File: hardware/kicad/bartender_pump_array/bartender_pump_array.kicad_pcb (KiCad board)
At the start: 2 copper layers, 56 x 61.8 mm, 43 parts, among them J1 Pump 1, J10 Pump 10, J11 12V INPUT, J12 Conn_01x12_Female, J2 Pump 2, J3 Pump 3, J4 Pump 4, J5 Pump 5, J6 Pump 6, J7 Pump 7, J8 Pump 8, J9 Pump 9, Q1 TIP120, Q10 TIP120, Q2 TIP120, Q3 TIP120, Q4 TIP120, Q5 TIP120, Q6 TIP120, Q7 TIP120, Q8 TIP120, Q9 TIP120

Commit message: Got wifi up and running, started work on the Mini
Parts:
- removed REF**: OSHW-Symbol_6.7x6mm_SilkScreen, Symbol:OSHW-Symbol_6.7x6mm_SilkScreen
- added H1: MountingHole_Pad, MountingHole:MountingHole_3.2mm_M3_Pad, F.Cu at (31.0, 45.5)
- added H2: MountingHole_Pad, MountingHole:MountingHole_3.2mm_M3_Pad, F.Cu at (62.9, 89.0)
- added R11: R_Small_US, Resistor_SMD:R_0603_1608Metric, B.Cu at (50.7, 85.2)
- added R12: R_Small_US, Resistor_SMD:R_0603_1608Metric, B.Cu at (50.7, 76.5)
- added R13: R_Small_US, Resistor_SMD:R_0603_1608Metric, B.Cu at (50.7, 67.8)
- added R14: R_Small_US, Resistor_SMD:R_0603_1608Metric, B.Cu at (50.7, 59.1)
- added R15: R_Small_US, Resistor_SMD:R_0603_1608Metric, B.Cu at (50.6, 50.5)
- added R16: R_Small_US, Resistor_SMD:R_0603_1608Metric, B.Cu at (59.2, 85.1)
- added R17: R_Small_US, Resistor_SMD:R_0603_1608Metric, B.Cu at (59.2, 76.5)
- added R18: R_Small_US, Resistor_SMD:R_0603_1608Metric, B.Cu at (59.2, 67.8)
- added R19: R_Small_US, Resistor_SMD:R_0603_1608Metric, B.Cu at (59.1, 59.8)
- added R20: R_Small_US, Resistor_SMD:R_0603_1608Metric, B.Cu at (59.1, 50.5)
- added U1: MCP23017_SO, Package_SO:SOIC-28W_7.5x17.9mm_P1.27mm, F.Cu at (34.9, 62.4)
- D1, D10, D2, D3, D4, D5, D6, D7, D8, D9: value DIODE -> 1N4148W; footprint Diode_THT:D_DO-41_SOD81_P5.08mm_Vertical_AnodeUp -> Diode_SMD:D_SOD-123; moved to B.Cu
- J1: value Pump 1 -> 1
- J10: value Pump 10 -> 10
- J11: value 12V INPUT -> 12V
- J12: value Conn_01x12_Female -> Conn_01x04_Female; footprint Connector_JST:JST_XH_B12B-XH-A_1x12_P2.50mm_Vertical -> Connector_JST:JST_XH_B4B-XH-A_1x04_P2.50mm_Vertical
- J2: value Pump 2 -> 2
- J3: value Pump 3 -> 3
- J4: value Pump 4 -> 4
- J5: value Pump 5 -> 5
- J6: value Pump 6 -> 6
- J7: value Pump 7 -> 7
- J8: value Pump 8 -> 8
- J9: value Pump 9 -> 9
- Q1, Q10, Q2, Q3, Q4, Q5, Q6, Q7, Q8, Q9: value TIP120 -> AO3400A; footprint Package_TO_SOT_THT:TO-220-3_Vertical -> Package_TO_SOT_SMD:SOT-23; moved to B.Cu
- R1, R10, R2, R3, R4, R5, R6, R7, R8, R9: footprint Resistor_THT:R_Axial_DIN0207_L6.3mm_D2.5mm_P5.08mm_Vertical -> Resistor_SMD:R_0603_1608Metric; moved to B.Cu
- moved R6 30.6 mm to (55.9, 85.1)
- moved R7 26.5 mm to (55.9, 76.5)
- moved J6 23.6 mm to (57.0, 83.2)
- moved R8 22.8 mm to (55.9, 67.8)
- moved J7 22.5 mm to (57.0, 74.5)
- moved J8 21.5 mm to (57.0, 65.9)
- moved J9 20.7 mm to (57.0, 57.2)
- moved J10 20.2 mm to (57.0, 48.6)
- moved R9 20.2 mm to (55.9, 59.8)
- moved D6 20.1 mm to (54.6, 81.9)
- moved J11 19.8 mm to (40.1, 80.4), turned to -90 degrees
- moved D7 18.9 mm to (54.7, 73.3)
- moved R10 18.2 mm to (55.9, 50.5)
- moved D8 18.1 mm to (54.7, 64.6)
- moved Q6 17.9 mm to (60.5, 82.0), turned to 0 degrees
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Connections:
- J12 pad 1: /P1 -> Net-(J12-Pad1)
- J12 pad 2: /P2 -> Net-(J12-Pad2)
- J12 pad 3: /P3 -> Net-(J12-Pad3)
- J12 pad 4: /P4 -> GND
- R1 pad 1: /P1 -> Net-(R1-Pad1)
- R10 pad 1: /P10 -> Net-(R10-Pad1)
- R2 pad 1: /P2 -> Net-(R2-Pad1)
- R3 pad 1: /P3 -> Net-(R3-Pad1)
- R4 pad 1: /P4 -> Net-(R4-Pad1)
- R5 pad 1: /P5 -> Net-(R5-Pad1)
- R6 pad 1: /P6 -> Net-(R6-Pad1)
- R7 pad 1: /P7 -> Net-(R7-Pad1)
- R8 pad 1: /P8 -> Net-(R8-Pad1)
- R9 pad 1: /P9 -> Net-(R9-Pad1)
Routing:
- net /12v: track 306.7 -> 144.7 mm, vias 1 -> 0
- net Net-(R6-Pad2): track 88.0 -> 4.23 mm
- net GND: track 219.7 -> 145.1 mm
- net Net-(R7-Pad2): track 74.9 -> 4.29 mm
- net Net-(R6-Pad1): track 0.00 -> 70.4 mm, vias 0 -> 1
- net Net-(R7-Pad1): track 0.00 -> 62.7 mm, vias 0 -> 1
- net Net-(R8-Pad2): track 61.7 -> 4.36 mm
- net Net-(R9-Pad1): track 0.00 -> 52.4 mm, vias 0 -> 1
- net Net-(R8-Pad1): track 0.00 -> 49.8 mm, vias 0 -> 1
- net Net-(R10-Pad1): track 0.00 -> 44.2 mm, vias 0 -> 1
- net Net-(Q9-Pad1): track 48.6 -> 5.56 mm
- net Net-(Q10-Pad1): track 35.4 -> 4.46 mm
- net Net-(J12-Pad2): track 0.00 -> 30.1 mm
- net Net-(J12-Pad1): track 0.00 -> 26.2 mm
- net Net-(J12-Pad3): track 0.00 -> 24.5 mm
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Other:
- board size 56 x 61.8 mm -> 39.9 x 51.9 mm
- net class Default removed
- board text added: "Bartender v1.3 Pump Board https://github.com/ dburnsii/bartender"
- board text removed: "+ -"
- board text removed: "Bartender v1.2 Pump Board https://github.com/ dburnsii/bartender"

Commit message: Updates for build, scale setup, new copy of pump board, etc
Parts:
- added R21: 1KR, Resistor_SMD:R_0603_1608Metric, F.Cu at (33.2, 59.8)
- added REF**: OSHW-Logo2_7.3x6mm_SilkScreen, Symbol:OSHW-Logo2_7.3x6mm_SilkScreen, F.Cu at (48.4, 89.7)
- H1, H2: footprint MountingHole:MountingHole_3.2mm_M3_Pad -> MountingHole:MountingHole_2.7mm_M2.5_Pad
- U1: value MCP23017_SO -> PCAL6416AHF,128; footprint Package_SO:SOIC-28W_7.5x17.9mm_P1.27mm -> PCAL6416AHF:QFN50P400X400X80-25N
- moved J12 15.3 mm to (32.8, 67.4), turned to -90 degrees
- moved Q1 8.30 mm to (43.9, 83.1), turned to 90 degrees
- moved Q3 8.14 mm to (43.9, 65.7), turned to 90 degrees
- moved Q2 8.08 mm to (44.0, 74.4), turned to 90 degrees
- moved Q5 8.07 mm to (44.0, 48.4), turned to 90 degrees
- moved D4 8.07 mm to (38.4, 56.5)
- moved H2 8.07 mm to (54.9, 90.0)
- moved R1 8.02 mm to (39.5, 85.9)
- moved Q4 8.02 mm to (44.0, 57.0), turned to 90 degrees
- moved R5 8.00 mm to (39.5, 51.3)
- moved D2 7.96 mm to (38.5, 74.0)
- moved D1 7.95 mm to (38.5, 82.7)
- moved R3 7.95 mm to (39.6, 68.5)
- moved D3 7.95 mm to (38.5, 65.3)
- moved R2 7.89 mm to (39.6, 77.2)
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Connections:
- D1 pad 2: Net-(J1-Pad1) -> Net-(D1-Pad2)
- D10 pad 2: Net-(J10-Pad1) -> Net-(D10-Pad2)
- D2 pad 2: Net-(J2-Pad1) -> Net-(D2-Pad2)
- D3 pad 2: Net-(J3-Pad1) -> Net-(D3-Pad2)
- D4 pad 2: Net-(J4-Pad1) -> Net-(D4-Pad2)
- D5 pad 2: Net-(J5-Pad1) -> Net-(D5-Pad2)
- D6 pad 2: Net-(J6-Pad1) -> Net-(D6-Pad2)
- D7 pad 2: Net-(J7-Pad1) -> Net-(D7-Pad2)
- D8 pad 2: Net-(J8-Pad1) -> Net-(D8-Pad2)
- D9 pad 2: Net-(J9-Pad1) -> Net-(D9-Pad2)
- J1 pad 1: Net-(J1-Pad1) -> Net-(D1-Pad2)
- J10 pad 1: Net-(J10-Pad1) -> Net-(D10-Pad2)
- J12 pad 1: Net-(J12-Pad1) -> +3V3
- J2 pad 1: Net-(J2-Pad1) -> Net-(D2-Pad2)
- J3 pad 1: Net-(J3-Pad1) -> Net-(D3-Pad2)
- J4 pad 1: Net-(J4-Pad1) -> Net-(D4-Pad2)
- J5 pad 1: Net-(J5-Pad1) -> Net-(D5-Pad2)
- J6 pad 1: Net-(J6-Pad1) -> Net-(D6-Pad2)
- J7 pad 1: Net-(J7-Pad1) -> Net-(D7-Pad2)
- J8 pad 1: Net-(J8-Pad1) -> Net-(D8-Pad2)
- J9 pad 1: Net-(J9-Pad1) -> Net-(D9-Pad2)
- Q1 pad 1: Net-(R1-Pad2) -> Net-(Q1-Pad1)
- Q1 pad 2: Net-(J1-Pad1) -> GND
- Q1 pad 3: GND -> Net-(D1-Pad2)
- Q10 pad 2: Net-(J10-Pad1) -> GND
- Q10 pad 3: GND -> Net-(D10-Pad2)
- Q2 pad 1: Net-(R2-Pad2) -> Net-(Q2-Pad1)
- Q2 pad 2: Net-(J2-Pad1) -> GND
- Q2 pad 3: GND -> Net-(D2-Pad2)
- Q3 pad 1: Net-(R3-Pad2) -> Net-(Q3-Pad1)
- Q3 pad 2: Net-(J3-Pad1) -> GND
- Q3 pad 3: GND -> Net-(D3-Pad2)
- Q4 pad 1: Net-(R4-Pad2) -> Net-(Q4-Pad1)
- Q4 pad 2: Net-(J4-Pad1) -> GND
- Q4 pad 3: GND -> Net-(D4-Pad2)
- Q5 pad 1: Net-(R5-Pad2) -> Net-(Q5-Pad1)
- Q5 pad 2: Net-(J5-Pad1) -> GND
- Q5 pad 3: GND -> Net-(D5-Pad2)
- Q6 pad 1: Net-(R6-Pad2) -> Net-(Q6-Pad1)
- Q6 pad 2: Net-(J6-Pad1) -> GND
- Q6 pad 3: GND -> Net-(D6-Pad2)
- Q7 pad 1: Net-(R7-Pad2) -> Net-(Q7-Pad1)
- Q7 pad 2: Net-(J7-Pad1) -> GND
- Q7 pad 3: GND -> Net-(D7-Pad2)
- Q8 pad 1: Net-(R8-Pad2) -> Net-(Q8-Pad1)
- Q8 pad 2: Net-(J8-Pad1) -> GND
- Q8 pad 3: GND -> Net-(D8-Pad2)
- Q9 pad 2: Net-(J9-Pad1) -> GND
- Q9 pad 3: GND -> Net-(D9-Pad2)
- R1 pad 2: Net-(R1-Pad2) -> Net-(Q1-Pad1)
- R11 pad 1: GND -> Net-(Q1-Pad1)
- R11 pad 2: Net-(R1-Pad2) -> GND
- R12 pad 1: GND -> Net-(Q2-Pad1)
- R12 pad 2: Net-(R2-Pad2) -> GND
- R13 pad 1: GND -> Net-(Q3-Pad1)
- R13 pad 2: Net-(R3-Pad2) -> GND
- R14 pad 1: GND -> Net-(Q4-Pad1)
- R14 pad 2: Net-(R4-Pad2) -> GND
- R15 pad 1: GND -> Net-(Q5-Pad1)
- R15 pad 2: Net-(R5-Pad2) -> GND
- R16 pad 1: GND -> Net-(Q6-Pad1)
- R16 pad 2: Net-(R6-Pad2) -> GND
- R17 pad 1: GND -> Net-(Q7-Pad1)
- R17 pad 2: Net-(R7-Pad2) -> GND
- R18 pad 1: GND -> Net-(Q8-Pad1)
- R18 pad 2: Net-(R8-Pad2) -> GND
- R19 pad 1: GND -> Net-(Q9-Pad1)
- R19 pad 2: Net-(Q9-Pad1) -> GND
- R2 pad 2: Net-(R2-Pad2) -> Net-(Q2-Pad1)
- R20 pad 1: GND -> Net-(Q10-Pad1)
- R20 pad 2: Net-(Q10-Pad1) -> GND
- R3 pad 2: Net-(R3-Pad2) -> Net-(Q3-Pad1)
- R4 pad 2: Net-(R4-Pad2) -> Net-(Q4-Pad1)
- R5 pad 2: Net-(R5-Pad2) -> Net-(Q5-Pad1)
- R6 pad 2: Net-(R6-Pad2) -> Net-(Q6-Pad1)
- R7 pad 2: Net-(R7-Pad2) -> Net-(Q7-Pad1)
- R8 pad 2: Net-(R8-Pad2) -> Net-(Q8-Pad1)
- U1 pad 10: unconnected-(U1-Pad10) -> Net-(R9-Pad1)
- U1 pad 11: unconnected-(U1-Pad11) -> Net-(R10-Pad1)
- U1 pad 12: Net-(J12-Pad3) -> unconnected-(U1-Pad12)
- U1 pad 13: Net-(J12-Pad2) -> unconnected-(U1-Pad13)
- U1 pad 18: unconnected-(U1-Pad18) -> GND
- U1 pad 19: unconnected-(U1-Pad19) -> Net-(J12-Pad2)
- U1 pad 20: unconnected-(U1-Pad20) -> Net-(J12-Pad3)
- U1 pad 21: Net-(R10-Pad1) -> +3V3
- U1 pad 22: Net-(R9-Pad1) -> unconnected-(U1-Pad22)
- U1 pad 23: unconnected-(U1-Pad23) -> +3V3
- U1 pad 24: unconnected-(U1-Pad24) -> Net-(R21-Pad1)
- U1 pad 9: Net-(J12-Pad1) -> GND
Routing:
- net GND: track 145.1 -> 207.1 mm, vias 0 -> 2
- net Net-(J12-Pad1): track 26.2 -> 0.00 mm
- net Net-(R9-Pad1): track 52.4 -> 39.0 mm
- net Net-(R10-Pad1): track 44.2 -> 31.4 mm
- net Net-(R1-Pad1): track 18.8 -> 30.8 mm
- net +3V3: track 0.00 -> 11.7 mm
- net Net-(R6-Pad1): track 70.4 -> 59.2 mm
- net Net-(R5-Pad1): track 19.0 -> 8.55 mm
- net Net-(R7-Pad1): track 62.7 -> 52.3 mm
- net Net-(R2-Pad1): track 12.7 -> 22.6 mm
- net Net-(J12-Pad3): track 24.5 -> 15.0 mm
- net Net-(J12-Pad2): track 30.1 -> 22.0 mm
- net Net-(R3-Pad1): track 7.48 -> 15.4 mm
- net Net-(J5-Pad1): track 6.88 -> 0.00 mm
- net Net-(D4-Pad2): track 0.00 -> 6.54 mm
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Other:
- board size 39.9 x 51.9 mm -> 31.5 x 51.9 mm
- board text added: "Bartender v1.4 Pump Board https://github.com/ dburnsii/bartender"
- board text removed: "Bartender v1.3 Pump Board https://github.com/ dburnsii/bartender"

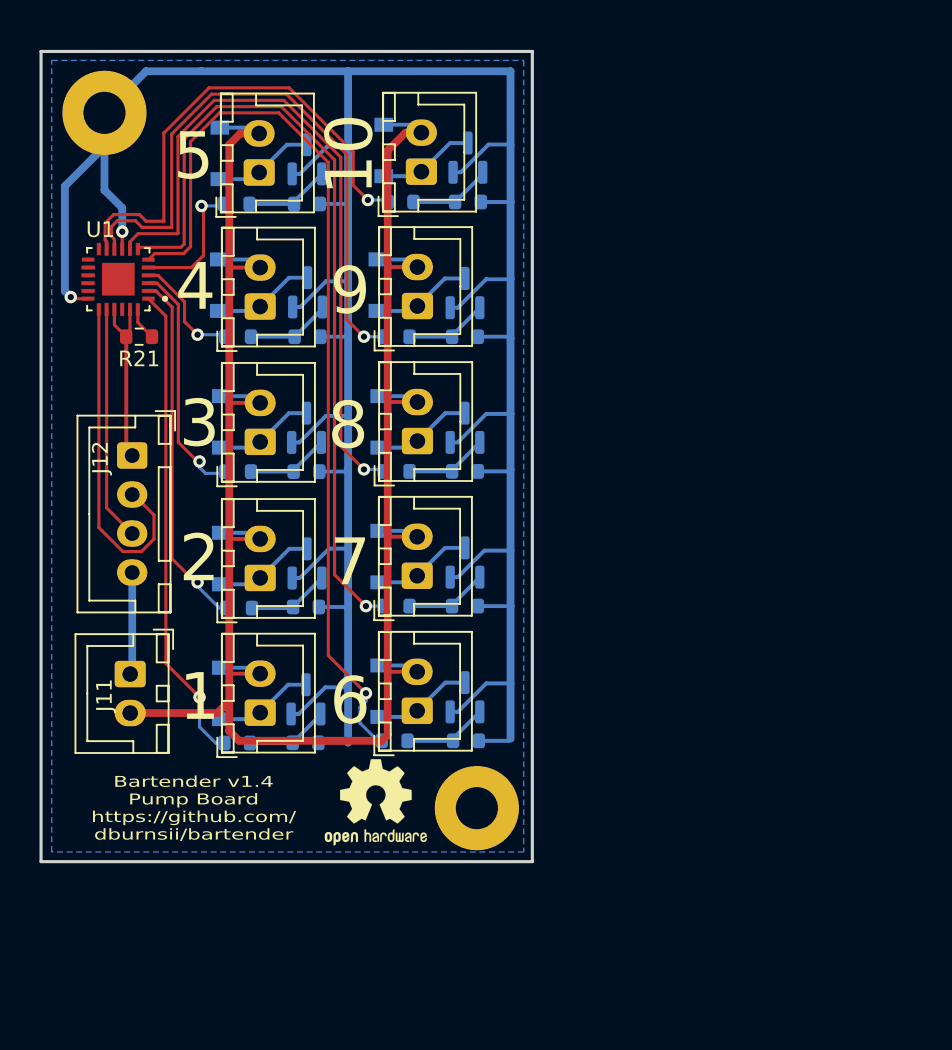
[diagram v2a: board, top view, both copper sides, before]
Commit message: Update to pull scale and valve from config, update boards
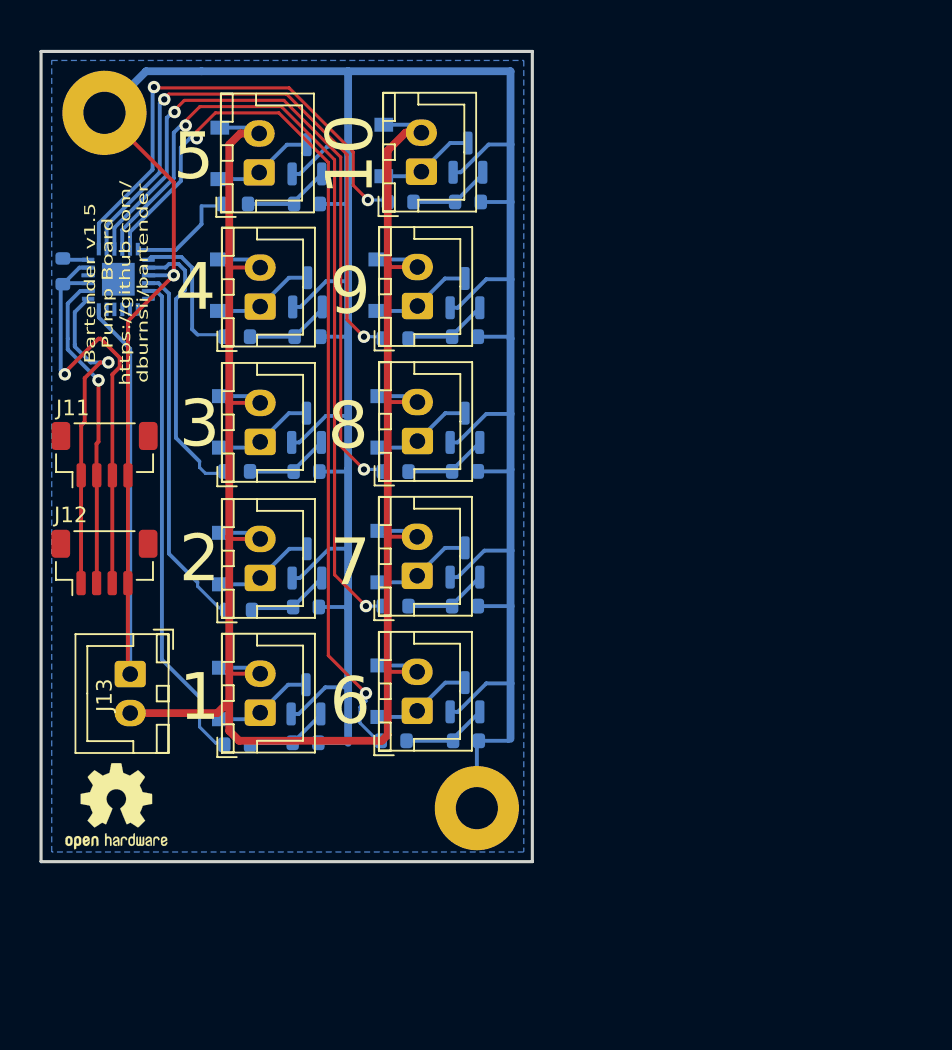
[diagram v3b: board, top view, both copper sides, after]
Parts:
- added J12: Conn_01x04_Female, Connector_JST:JST_SH_BM04B-SRSS-TB_1x04-1MP_P1.00mm_Vertical, F.Cu at (31.0, 74.3)
- J11: renamed from J12; footprint Connector_JST:JST_XH_B4B-XH-A_1x04_P2.50mm_Vertical -> Connector_JST:JST_SH_BM04B-SRSS-TB_1x04-1MP_P1.00mm_Vertical
- R21, U1: moved to B.Cu
- moved R10 36.3 mm to (39.5, 86.0)
- moved R1 36.2 mm to (50.0, 51.2)
- moved R6 35.9 mm to (39.4, 51.3)
- moved R5 35.9 mm to (49.5, 85.7)
- moved R9 20.2 mm to (39.6, 77.3)
- moved R7 20.1 mm to (39.5, 59.8)
- moved R4 20.0 mm to (49.7, 77.1)
- moved R2 20.0 mm to (49.7, 59.9)
- moved REF** 16.6 mm to (31.8, 89.9)
- moved R8 10.2 mm to (39.5, 68.5)
- moved R3 10.1 mm to (49.7, 68.5)
- moved R21 6.44 mm to (28.3, 55.6), turned to -90 degrees
- moved J11 1.77 mm to (31.0, 67.4), turned to 0 degrees
- turned U1 to -90 degrees
- renumbered D10 to D1, D1 to D10, D9 to D2, D8 to D3, D7 to D4, D6 to D5, D5 to D6, D4 to D7, D3 to D8, D2 to D9, H2 to H1, H1 to H2, J10 to J1, J1 to J10, J11 to J13, J9 to J2, J8 to J3, J7 to J4, J6 to J5, J5 to J6, J4 to J7, J3 to J8, J2 to J9, Q10 to Q1, Q1 to Q10, Q9 to Q2, Q8 to Q3, Q7 to Q4, Q6 to Q5, Q5 to Q6, Q4 to Q7, Q3 to Q8, Q2 to Q9, R20 to R11, R19 to R12, R18 to R13, R17 to R14, R16 to R15, R15 to R16, R14 to R17, R13 to R18, R12 to R19, R11 to R20
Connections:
- J11 pad 1: +3V3 -> Net-(J11-Pad1)
- J11 pad 2: Net-(J12-Pad2) -> Net-(J11-Pad2)
- J11 pad 3: Net-(J12-Pad3) -> +3V3
- Q1 pad 1: Net-(Q10-Pad1) -> Net-(R1-Pad2)
- Q10 pad 1: Net-(Q1-Pad1) -> Net-(Q10-Pad1)
- Q2 pad 1: Net-(Q9-Pad1) -> Net-(R2-Pad2)
- Q3 pad 1: Net-(Q8-Pad1) -> Net-(R3-Pad2)
- Q4 pad 1: Net-(Q7-Pad1) -> Net-(R4-Pad2)
- Q5 pad 1: Net-(Q6-Pad1) -> Net-(R5-Pad2)
- Q6 pad 1: Net-(Q5-Pad1) -> Net-(Q6-Pad1)
- Q7 pad 1: Net-(Q4-Pad1) -> Net-(Q7-Pad1)
- Q8 pad 1: Net-(Q3-Pad1) -> Net-(Q8-Pad1)
- Q9 pad 1: Net-(Q2-Pad1) -> Net-(Q9-Pad1)
- R1 pad 2: Net-(Q1-Pad1) -> Net-(R1-Pad2)
- R11 pad 1: Net-(Q10-Pad1) -> Net-(R1-Pad2)
- R12 pad 1: Net-(Q9-Pad1) -> Net-(R2-Pad2)
- R13 pad 1: Net-(Q8-Pad1) -> Net-(R3-Pad2)
- R14 pad 1: Net-(Q7-Pad1) -> Net-(R4-Pad2)
- R15 pad 1: Net-(Q6-Pad1) -> Net-(R5-Pad2)
- R16 pad 1: Net-(Q5-Pad1) -> Net-(Q6-Pad1)
- R17 pad 1: Net-(Q4-Pad1) -> Net-(Q7-Pad1)
- R18 pad 1: Net-(Q3-Pad1) -> Net-(Q8-Pad1)
- R19 pad 1: Net-(Q2-Pad1) -> Net-(Q9-Pad1)
- R2 pad 2: Net-(Q2-Pad1) -> Net-(R2-Pad2)
- R20 pad 1: Net-(Q1-Pad1) -> Net-(Q10-Pad1)
- R3 pad 2: Net-(Q3-Pad1) -> Net-(R3-Pad2)
- R4 pad 2: Net-(Q4-Pad1) -> Net-(R4-Pad2)
- R5 pad 2: Net-(Q5-Pad1) -> Net-(R5-Pad2)
- U1 pad 19: Net-(J12-Pad2) -> Net-(J11-Pad1)
- U1 pad 20: Net-(J12-Pad3) -> Net-(J11-Pad2)
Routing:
- net Net-(R6-Pad1): track 59.2 -> 7.44 mm, vias 1 -> 0
- net Net-(R5-Pad1): track 8.55 -> 58.3 mm, vias 1 -> 2
- net Net-(R4-Pad1): track 7.30 -> 51.8 mm, vias 1 -> 2
- net Net-(R7-Pad1): track 52.3 -> 9.43 mm, vias 1 -> 0
- net GND: track 207.1 -> 246.6 mm, vias 2 -> 1
- net Net-(R3-Pad1): track 15.4 -> 44.9 mm, vias 1 -> 2
- net Net-(R8-Pad1): track 44.8 -> 18.0 mm, vias 1 -> 0
- net Net-(J12-Pad2): track 22.0 -> 0.00 mm
- net Net-(J11-Pad1): track 0.00 -> 21.2 mm, vias 0 -> 1
- net Net-(J11-Pad2): track 0.00 -> 20.5 mm, vias 0 -> 1
- net +3V3: track 11.7 -> 29.4 mm, vias 0 -> 1
- net Net-(R9-Pad1): track 39.0 -> 23.1 mm, vias 1 -> 0
- net Net-(R2-Pad1): track 22.6 -> 38.0 mm, vias 1 -> 2
- net Net-(J12-Pad3): track 15.0 -> 0.00 mm
- net Net-(Q5-Pad1): track 5.52 -> 0.00 mm
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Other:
- board text added: "Bartender v1.5 Pump Board https://github.com/ dburnsii/bartender"
- board text removed: "Bartender v1.4 Pump Board https://github.com/ dburnsii/bartender"
